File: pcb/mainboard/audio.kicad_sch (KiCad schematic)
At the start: 29 parts, among them J401 AudioJack3, U201 MIMX8MN6DVTJZAA, U402 FSA2269UMX, U403 WM8978

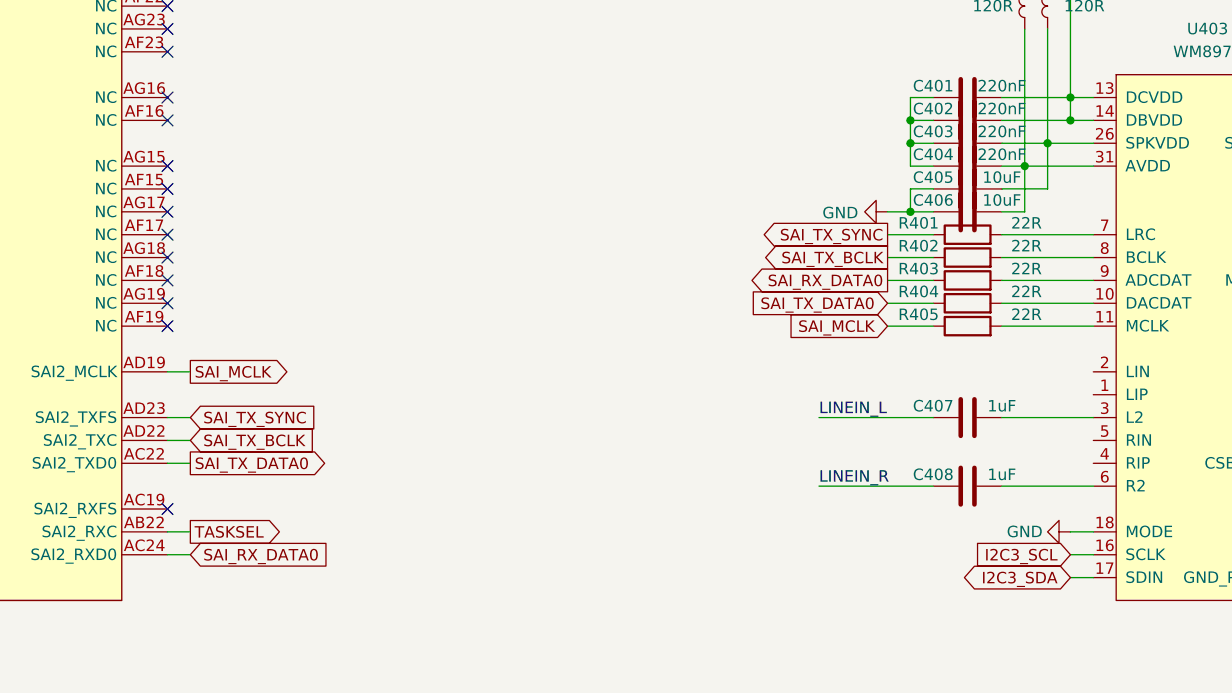
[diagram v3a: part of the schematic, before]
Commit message: Routing mainboard in progress, schematics fixes
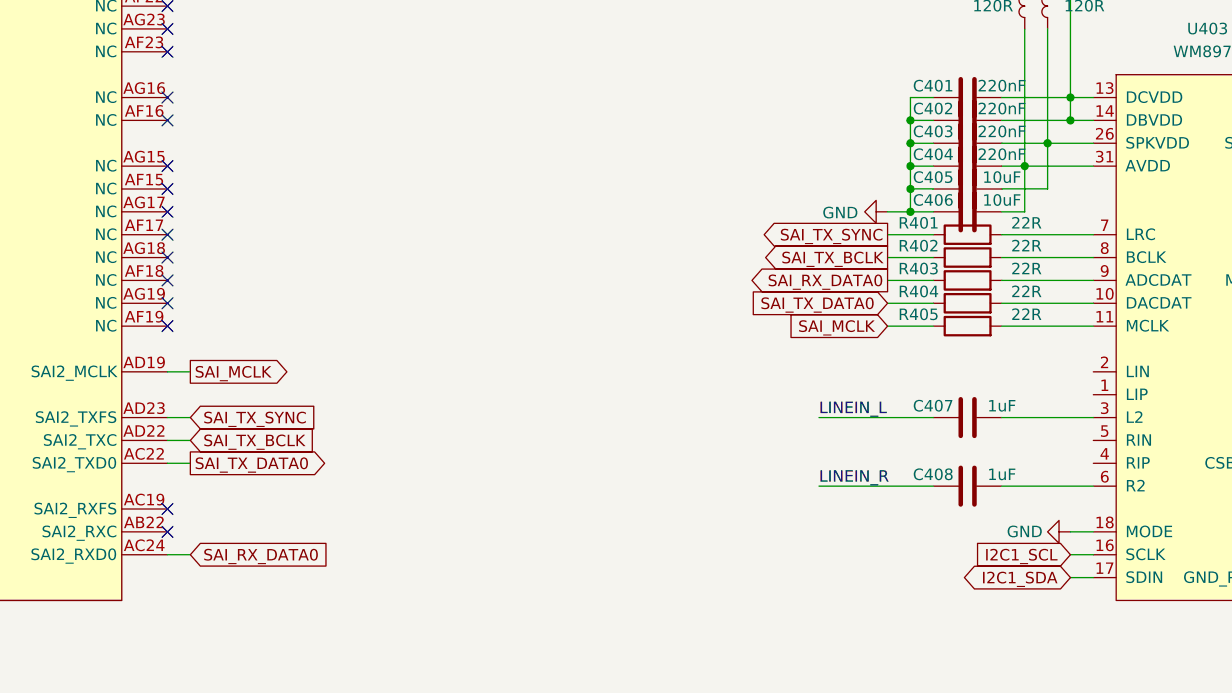
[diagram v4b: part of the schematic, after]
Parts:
- LS401: footprint Buzzer_Beeper:Speaker_CUI_CMR-1206S-67 -> Buzzer_Beeper:Buzzer_CUI_CPT-9019S-SMT
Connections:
- net GND: now also C401.2, C402.2, C403.2, C404.2
- net TASKSEL: no longer U201.AB22 (SAI2_RXC)
- net I2C3_SCL renamed I2C1_SCL
- net I2C3_SDA renamed I2C1_SDA
- no-connect marks 40 -> 41
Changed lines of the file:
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@@
   (junction (at 231.14 144.78) (diameter 0) (color 0 0 0 0)
   )
+  (junction (at 170.18 106.68) (diameter 0) (color 0 0 0 0)
+  )
   (junction (at 213.36 63.5) (diameter 0) (color 0 0 0 0)
   )
@@
   )
   (junction (at 170.18 99.06) (diameter 0.9144) (color 0 0 0 0)
+  )
+  (junction (at 170.18 104.14) (diameter 0) (color 0 0 0 0)
   )
   (junction (at 187.96 96.52) (diameter 0.9144) (color 0 0 0 0)
@@
   (no_connect (at 46.99 104.14))
   (no_connect (at 46.99 86.36))
+  (no_connect (at 87.63 144.78))
   (no_connect (at 46.99 78.74))
   (no_connect (at 46.99 76.2))
@@
   (no_connect (at 46.99 73.66))
   (no_connect (at 87.63 142.24))
-  (wire (pts (xy 87.63 144.78) (xy 90.17 144.78))
-    (stroke (width 0) (type default) (color 0 0 0 0))
-  )
   (wire (pts (xy 187.96 149.86) (xy 190.5 149.86))
     (stroke (width 0) (type solid) (color 0 0 0 0))
@@
   )
   (wire (pts (xy 87.63 127) (xy 90.17 127))
+    (stroke (width 0) (type default) (color 0 0 0 0))
+  )
+  (wire (pts (xy 170.18 104.14) (xy 170.18 106.68))
     (stroke (width 0) (type default) (color 0 0 0 0))
   )
@@
     )
   )
-  (global_label "I2C3_SCL" (shape input) (at 187.96 147.32 180)
+  (global_label "I2C1_SCL" (shape input) (at 187.96 147.32 180)
     (effects (font (size 1.27 1.27)) (justify right))
     (property "Intersheet References" "${INTERSHEET_REFS}" (id 0) (at 144.78 7.62 0)
@@
     )
   )
-  (global_label "TASKSEL" (shape output) (at 90.17 144.78 0) (fields_autoplaced)
-    (effects (font (size 1.27 1.27)) (justify left))
-    (property "Intersheet References" "${INTERSHEET_REFS}" (id 0) (at 100.696 144.7006 0)
-      (effects (font (size 1.27 1.27)) (justify left) hide)
-    )
-  )
   (global_label "SAI_MCLK" (shape output) (at 90.17 127 0)
     (effects (font (size 1.27 1.27)) (justify left))
@@
     )
   )
-  (global_label "I2C3_SDA" (shape bidirectional) (at 187.96 149.86 180)
+  (global_label "I2C1_SDA" (shape bidirectional) (at 187.96 149.86 180)
     (effects (font (size 1.27 1.27)) (justify right))
     (property "Intersheet References" "${INTERSHEET_REFS}" (id 0) (at 144.78 7.62 0)
@@
       (effects (font (size 1.27 1.27)) (justify left))
     )
-    (property "Footprint" "Buzzer_Beeper:Speaker_CUI_CMR-1206S-67" (id 2) (at 259.08 147.32 0)
-      (effects (font (size 1.27 1.27)) hide)
-    )
+    (property "Footprint" "Buzzer_Beeper:Buzzer_CUI_CPT-9019S-SMT" (id 2) (at 259.08 147.32 0)
+      (effects (font (size 1.27 1.27)) hide)
+    )
